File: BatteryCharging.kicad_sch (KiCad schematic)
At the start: 15 parts, among them J6 Battery Connector, Q2 AO3401A, U5 MCP73831-2-OT, U6 74AHCT1G04, U7 LC709203FXE-05MH

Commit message: Rev C, I think
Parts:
- R9: value 4.7k -> 2k; footprint Resistor_SMD:R_0603_1608Metric_Pad0.98x0.95mm_HandSolder -> Resistor_SMD:R_0603_1608Metric; Rate Approx 250mA -> Approx 500mA
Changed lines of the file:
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@@
     (in_bom yes) (on_board yes) (fields_autoplaced)
     (property "Reference" "R9" (id 0) (at 185.42 51.9323 90))
-    (property "Value" "4.7k" (id 1) (at 185.42 54.7074 90))
-    (property "Footprint" "Resistor_SMD:R_0603_1608Metric_Pad0.98x0.95mm_HandSolder" (id 2) (at 185.42 61.468 90)
+    (property "Value" "2k" (id 1) (at 185.42 54.7074 90))
+    (property "Footprint" "Resistor_SMD:R_0603_1608Metric" (id 2) (at 185.42 61.468 90)
       (effects (font (size 1.27 1.27)) hide)
     )
@@
       (effects (font (size 1.27 1.27)) hide)
     )
-    (property "Rate" "Approx 250mA" (id 4) (at 185.42 57.4825 90)
+    (property "Rate" "Approx 500mA" (id 4) (at 185.42 57.4825 90)
       (effects (font (size 1.27 1.27) italic))
     )

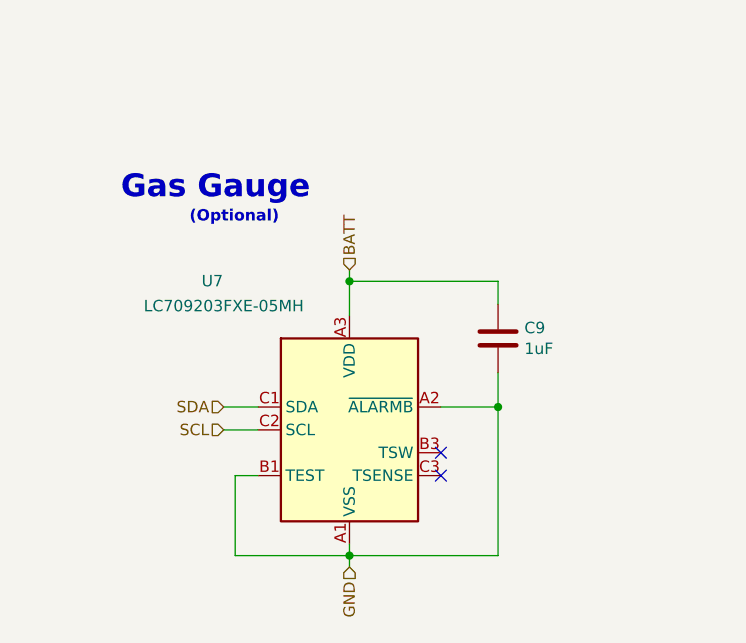
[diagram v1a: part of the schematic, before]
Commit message: Remove Gas Gauge IC
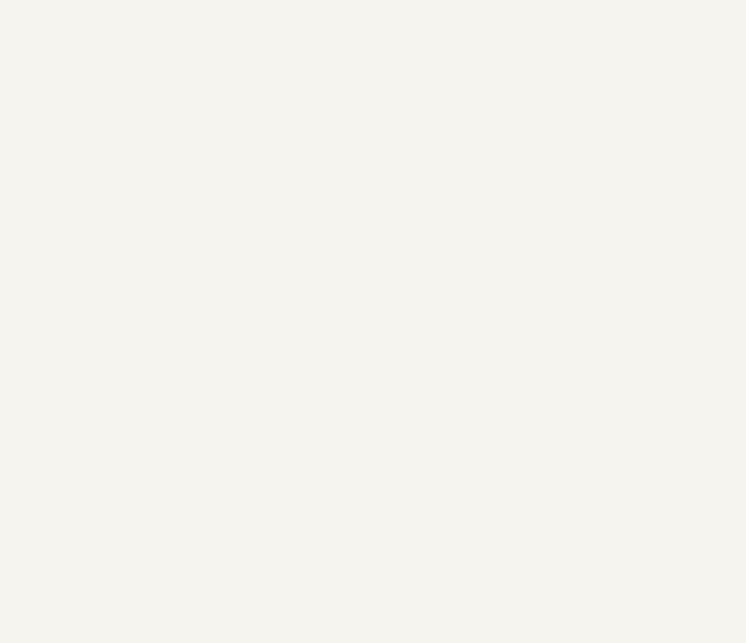
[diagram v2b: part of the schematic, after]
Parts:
- removed C9: 1uF, Capacitor_SMD:C_0603_1608Metric, symbol Device:C
- removed U7: LC709203FXE-05MH, MikeFootprintLib:WLCSP9-1.60x1.76mm, symbol MikeLib:LC709203FXE-05MH
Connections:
- no-connect marks 2 -> 0
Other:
- note removed: "Gas Gauge"
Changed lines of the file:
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@@
   (junction (at 44.45 52.07) (diameter 0) (color 0 0 0 0)
   )
-  (junction (at 53.34 166.37) (diameter 0) (color 0 0 0 0)
-  )
   (junction (at 143.51 59.69) (diameter 0) (color 0 0 0 0)
   )
-  (junction (at 53.34 135.89) (diameter 0) (color 0 0 0 0)
-  )
   (junction (at 167.64 43.18) (diameter 0) (color 0 0 0 0)
   )
@@
   (junction (at 53.34 62.23) (diameter 0) (color 0 0 0 0)
   )
-  (junction (at 69.85 149.86) (diameter 0) (color 0 0 0 0)
-  )
-  (no_connect (at 63.5 154.94))
-  (no_connect (at 63.5 157.48))
   (wire (pts (xy 59.69 52.07) (xy 69.85 52.07))
     (stroke (width 0) (type default) (color 0 0 0 0))
@@
     (stroke (width 0) (type default) (color 0 0 0 0))
   )
-  (wire (pts (xy 39.37 152.4) (xy 43.18 152.4))
-    (stroke (width 0) (type default) (color 0 0 0 0))
-  )
-  (wire (pts (xy 53.34 166.37) (xy 69.85 166.37))
-    (stroke (width 0) (type default) (color 0 0 0 0))
-  )
   (wire (pts (xy 219.71 59.69) (xy 242.57 59.69))
     (stroke (width 0) (type default) (color 0 0 0 0))
@@
     (stroke (width 0) (type default) (color 0 0 0 0))
   )
-  (wire (pts (xy 63.5 149.86) (xy 69.85 149.86))
-    (stroke (width 0) (type default) (color 0 0 0 0))
-  )
   (wire (pts (xy 156.21 57.15) (xy 167.64 57.15))
     (stroke (width 0) (type default) (color 0 0 0 0))
   )
-  (wire (pts (xy 53.34 135.89) (xy 53.34 139.7))
-    (stroke (width 0) (type default) (color 0 0 0 0))
-  )
   (wire (pts (xy 156.21 62.23) (xy 165.1 62.23))
     (stroke (width 0) (type default) (color 0 0 0 0))
   )
-  (wire (pts (xy 69.85 138.43) (xy 69.85 135.89))
-    (stroke (width 0) (type default) (color 0 0 0 0))
-  )
-  (wire (pts (xy 69.85 166.37) (xy 69.85 149.86))
-    (stroke (width 0) (type default) (color 0 0 0 0))
-  )
   (wire (pts (xy 58.42 52.07) (xy 59.69 52.07))
     (stroke (width 0) (type default) (color 0 0 0 0))
@@
     (stroke (width 0) (type default) (color 0 0 0 0))
   )
-  (wire (pts (xy 40.64 157.48) (xy 40.64 166.37))
-    (stroke (width 0) (type default) (color 0 0 0 0))
-  )
   (wire (pts (xy 44.45 45.72) (xy 44.45 52.07))
     (stroke (width 0) (type default) (color 0 0 0 0))
@@
     (stroke (width 0) (type default) (color 0 0 0 0))
   )
-  (wire (pts (xy 39.37 149.86) (xy 43.18 149.86))
-    (stroke (width 0) (type default) (color 0 0 0 0))
-  )
-  (wire (pts (xy 53.34 165.1) (xy 53.34 166.37))
-    (stroke (width 0) (type default) (color 0 0 0 0))
-  )
-  (wire (pts (xy 53.34 166.37) (xy 53.34 167.64))
-    (stroke (width 0) (type default) (color 0 0 0 0))
-  )
-  (wire (pts (xy 69.85 135.89) (xy 53.34 135.89))
-    (stroke (width 0) (type default) (color 0 0 0 0))
-  )
   (wire (pts (xy 229.87 38.1) (xy 223.52 38.1))
     (stroke (width 0) (type default) (color 0 0 0 0))
@@
     (stroke (width 0) (type default) (color 0 0 0 0))
   )
-  (wire (pts (xy 69.85 146.05) (xy 69.85 149.86))
-    (stroke (width 0) (type default) (color 0 0 0 0))
-  )
-  (wire (pts (xy 43.18 157.48) (xy 40.64 157.48))
-    (stroke (width 0) (type default) (color 0 0 0 0))
-  )
   (wire (pts (xy 242.57 50.8) (xy 242.57 46.99))
     (stroke (width 0) (type default) (color 0 0 0 0))
@@
   )
   (wire (pts (xy 143.51 54.61) (xy 143.51 59.69))
-    (stroke (width 0) (type default) (color 0 0 0 0))
-  )
-  (wire (pts (xy 40.64 166.37) (xy 53.34 166.37))
-    (stroke (width 0) (type default) (color 0 0 0 0))
-  )
-  (wire (pts (xy 53.34 134.62) (xy 53.34 135.89))
     (stroke (width 0) (type default) (color 0 0 0 0))
   )
@@
   (text "Battery Charging" (at 133.35 31.75 0)
     (effects (font (size 1.27 1.27) bold) (justify left bottom))
-  )
-  (text "Gas Gauge" (at 27.94 127 0)
-    (effects (font (size 2.54 2.54) (thickness 1.016) bold) (justify left bottom))
   )
   (text "V_{High} is equal to 5V bus if 5V present, else V_{Batt}."
@@
     (effects (font (size 2.54 2.54) (thickness 1.016) bold) (justify left bottom))
   )
-  (text "(Optional)" (at 35.56 129.54 0)
-    (effects (font (size 1.27 1.27) bold) (justify left bottom))
-  )
   (label "ProgSink" (at 167.64 59.69 0)
     (effects (font (size 1.27 1.27)) (justify left bottom))
@@
     (effects (font (size 1.27 1.27)) (justify left))
   )
-  (hierarchical_label "SCL" (shape input) (at 39.37 152.4 180)
-    (effects (font (size 1.27 1.27)) (justify right))
-  )
-  (hierarchical_label "BATT" (shape input) (at 53.34 134.62 90)
-    (effects (font (size 1.27 1.27)) (justify left))
-  )
   (hierarchical_label "GND" (shape input) (at 165.1 62.23 270)
     (effects (font (size 1.27 1.27)) (justify right))
@@
     (effects (font (size 1.27 1.27)) (justify right))
   )
-  (hierarchical_label "SDA" (shape input) (at 39.37 149.86 180)
-    (effects (font (size 1.27 1.27)) (justify right))
-  )
   (hierarchical_label "BATT" (shape input) (at 223.52 34.29 90)
     (effects (font (size 1.27 1.27)) (justify left))
@@
   )
   (hierarchical_label "GND" (shape input) (at 172.72 50.8 270)
-    (effects (font (size 1.27 1.27)) (justify right))
-  )
-  (hierarchical_label "GND" (shape input) (at 53.34 167.64 270)
     (effects (font (size 1.27 1.27)) (justify right))
   )
@@
     (pin "2")
   )
-  (symbol (lib_id "MikeLib:LC709203FXE-05MH") (at 53.34 152.4 0) (unit 1)
-    (in_bom yes) (on_board yes)
-    (property "Reference" "U7" (id 0) (at 38.1 135.8604 0))
-    (property "Value" "LC709203FXE-05MH" (id 1) (at 39.37 138.6355 0))
-    (property "Footprint" "MikeFootprintLib:WLCSP9-1.60x1.76mm" (id 2) (at 53.34 166.37 0)
-      (effects (font (size 1.27 1.27)) hide)
-    )
-    (property "Datasheet" "https://www.onsemi.com/pub/Collateral/LC709203F-D.PDF" (id 3) (at 52.07 154.94 0)
-      (effects (font (size 1.27 1.27)) hide)
-    )
-    (pin "A1")
-    (pin "A2")
-    (pin "A3")
-    (pin "B1")
-    (pin "B2")
-    (pin "B3")
-    (pin "C1")
-    (pin "C2")
-    (pin "C3")
-  )
   (symbol (lib_id "Device:R") (at 185.42 59.69 90) (unit 1)
     (in_bom yes) (on_board yes) (fields_autoplaced)
@@
       (effects (font (size 1.27 1.27)) hide)
     )
-    (pin "1")
-    (pin "2")
-  )
-  (symbol (lib_id "Device:C") (at 69.85 142.24 0) (unit 1)
-    (in_bom yes) (on_board yes)
-    (property "Reference" "C9" (id 0) (at 72.771 141.0716 0)
-      (effects (font (size 1.27 1.27)) (justify left))
-    )
-    (property "Value" "1uF" (id 1) (at 72.771 143.383 0)
-      (effects (font (size 1.27 1.27)) (justify left))
-    )
-    (property "Footprint" "Capacitor_SMD:C_0603_1608Metric" (id 2) (at 70.8152 146.05 0)
-      (effects (font (size 1.27 1.27)) hide)
-    )
-    (property "Datasheet" "~" (id 3) (at 69.85 142.24 0)
-      (effects (font (size 1.27 1.27)) hide)
-    )
